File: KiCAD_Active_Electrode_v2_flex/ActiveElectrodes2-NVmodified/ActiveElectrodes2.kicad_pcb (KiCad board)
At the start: 2 copper layers, 10.2 x 10.2 mm, 17 parts, among them IC1 AD8606ACBZ, IC2 AD8606ACBZ, J1 Conn_01x04_Male, J2 Conn_01x01_Male

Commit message: LPF updated
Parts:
- added C7: 0.1uF, Capacitor_SMD:C_0402_1005Metric, F.Cu at (45.9, 26.5)
- added C8: 0.1uF, Capacitor_SMD:C_0402_1005Metric, F.Cu at (49.8, 24.4)
- added R8: 20k, Capacitor_SMD:C_0402_1005Metric, F.Cu at (47.1, 26.0)
- added R9: 20k, Capacitor_SMD:C_0402_1005Metric, F.Cu at (48.2, 25.2)
- moved J1 0.55 mm to (46.1, 31.1)
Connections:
- IC2 pad A3: Net-(IC2-PadA3) -> 4th_Out
- IC2 pad B3: Net-(IC2-PadB3) -> 4th_Out
- IC2 pad C3: Net-(IC2-PadC3) -> 4th+
- J1 pad 4: 2nd_Out -> 4th_Out
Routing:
- net GND: track 25.9 -> 17.6 mm, vias 5 -> 3
- net 4th_Out: track 0.00 -> 7.26 mm, vias 0 -> 2
- net 4th+: track 0.00 -> 3.14 mm
- net Net-(C7-Pad2): track 0.00 -> 2.53 mm
- net 2nd_Out: track 6.09 -> 6.25 mm, vias 1 -> 2
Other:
- board size 10.2 x 10.2 mm -> 11.6 x 11.6 mm

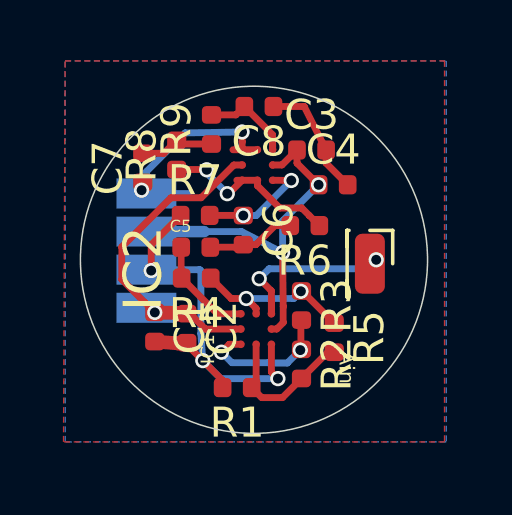
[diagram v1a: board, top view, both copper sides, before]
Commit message: Fixed with HPF first
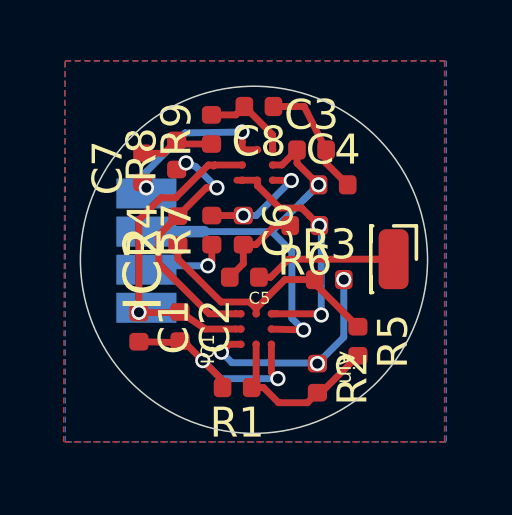
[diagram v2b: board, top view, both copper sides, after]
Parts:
- moved C5 1.90 mm to (49.3, 30.1), turned to 0 degrees
- moved R4 1.69 mm to (47.1, 28.6), turned to 90 degrees
- moved R3 1.27 mm to (52.2, 30.2), turned to 0 degrees
- moved J2 0.80 mm to (54.3, 29.5)
- moved R5 0.80 mm to (53.1, 32.2)
- moved R7 0.74 mm to (48.2, 28.5), turned to 90 degrees
- moved R2 0.71 mm to (51.8, 33.5)
- moved C1 0.53 mm to (45.8, 31.8)
- moved C2 0.24 mm to (47.2, 31.7)
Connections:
- C5 pad 2: amplifier_out -> Electrode_in
- IC1 pad C3: Electrode_in -> 2nd_Out
- R8 pad 1: 2nd_Out -> amplifier_out
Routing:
- net amplifier_out: track 3.50 -> 9.02 mm, vias 0 -> 2
- net GND: track 17.6 -> 14.3 mm
- net Net-(IC1-PadB3): track 5.58 -> 8.44 mm, vias 2 -> 0
- net Net-(IC1-PadA1): track 4.70 -> 7.28 mm, vias 2 -> 3
- net 2nd_Out: track 6.25 -> 8.35 mm
- net 4th_Out: track 7.26 -> 5.55 mm
- net VSS: track 12.2 -> 13.8 mm
- net Electrode_in: track 5.95 -> 4.81 mm, vias 2 -> 0
- net Net-(IC1-PadB1): track 5.00 -> 5.90 mm

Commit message: Changed
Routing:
- net GND: vias 3 -> 4

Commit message: Updated
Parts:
- IC2: value AD8606ACBZ -> (none)
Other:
- board text added: "preamp design yeolab 11.20.19"
- board text removed: "preamp design yeolab 8.19.19"
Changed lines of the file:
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@@
   (page A4)
   (layers
-    (0 F.Cu signal)
-    (31 B.Cu signal)
+    (0 F.Cu signal hide)
+    (31 B.Cu signal hide)
     (32 B.Adhes user hide)
     (33 F.Adhes user hide)
@@
       (effects (font (size 0.4 0.4) (thickness 0.1)))
     )
-    (fp_text value AD8606ACBZ (at -3.4544 -3.81 90) (layer F.SilkS) hide
-      (effects (font (size 1.27 1.27) (thickness 0.254)))
+    (fp_text value "" (at 2.57 5.36 90) (layer F.SilkS) hide
+      (effects (font (size 0.5 0.5) (thickness 0.1)))
     )
     (fp_circle (center -0.52 -0.52) (end -0.35 -0.53) (layer F.SilkS) (width 0.15))
@@
     )
   )
-  (gr_text "preamp design\nyeolab\n8.19.19" (at 49.68 26.31) (layer B.SilkS)
+  (gr_text "preamp design\nyeolab\n11.20.19" (at 49.68 26.31) (layer B.SilkS)
     (effects (font (size 0.5 0.5) (thickness 0.1)) (justify mirror))
   )
